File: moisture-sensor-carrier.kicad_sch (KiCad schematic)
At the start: 56 parts, among them J1 USB-C receptacle, J2 Battery - Adafruit 1578, J3 Solar panel, J4 SWD 10p 1.27mm, J5 Antenna feed, U1 nRF54L15-QFAA, U2 nPM1300-QEAA, U3 FDC1004, U4 SHT45-AD1F, X1 CM8V-T1A 32.768kHz CL=7pF 20p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, X2 FA-128 32MHz CL=8pF

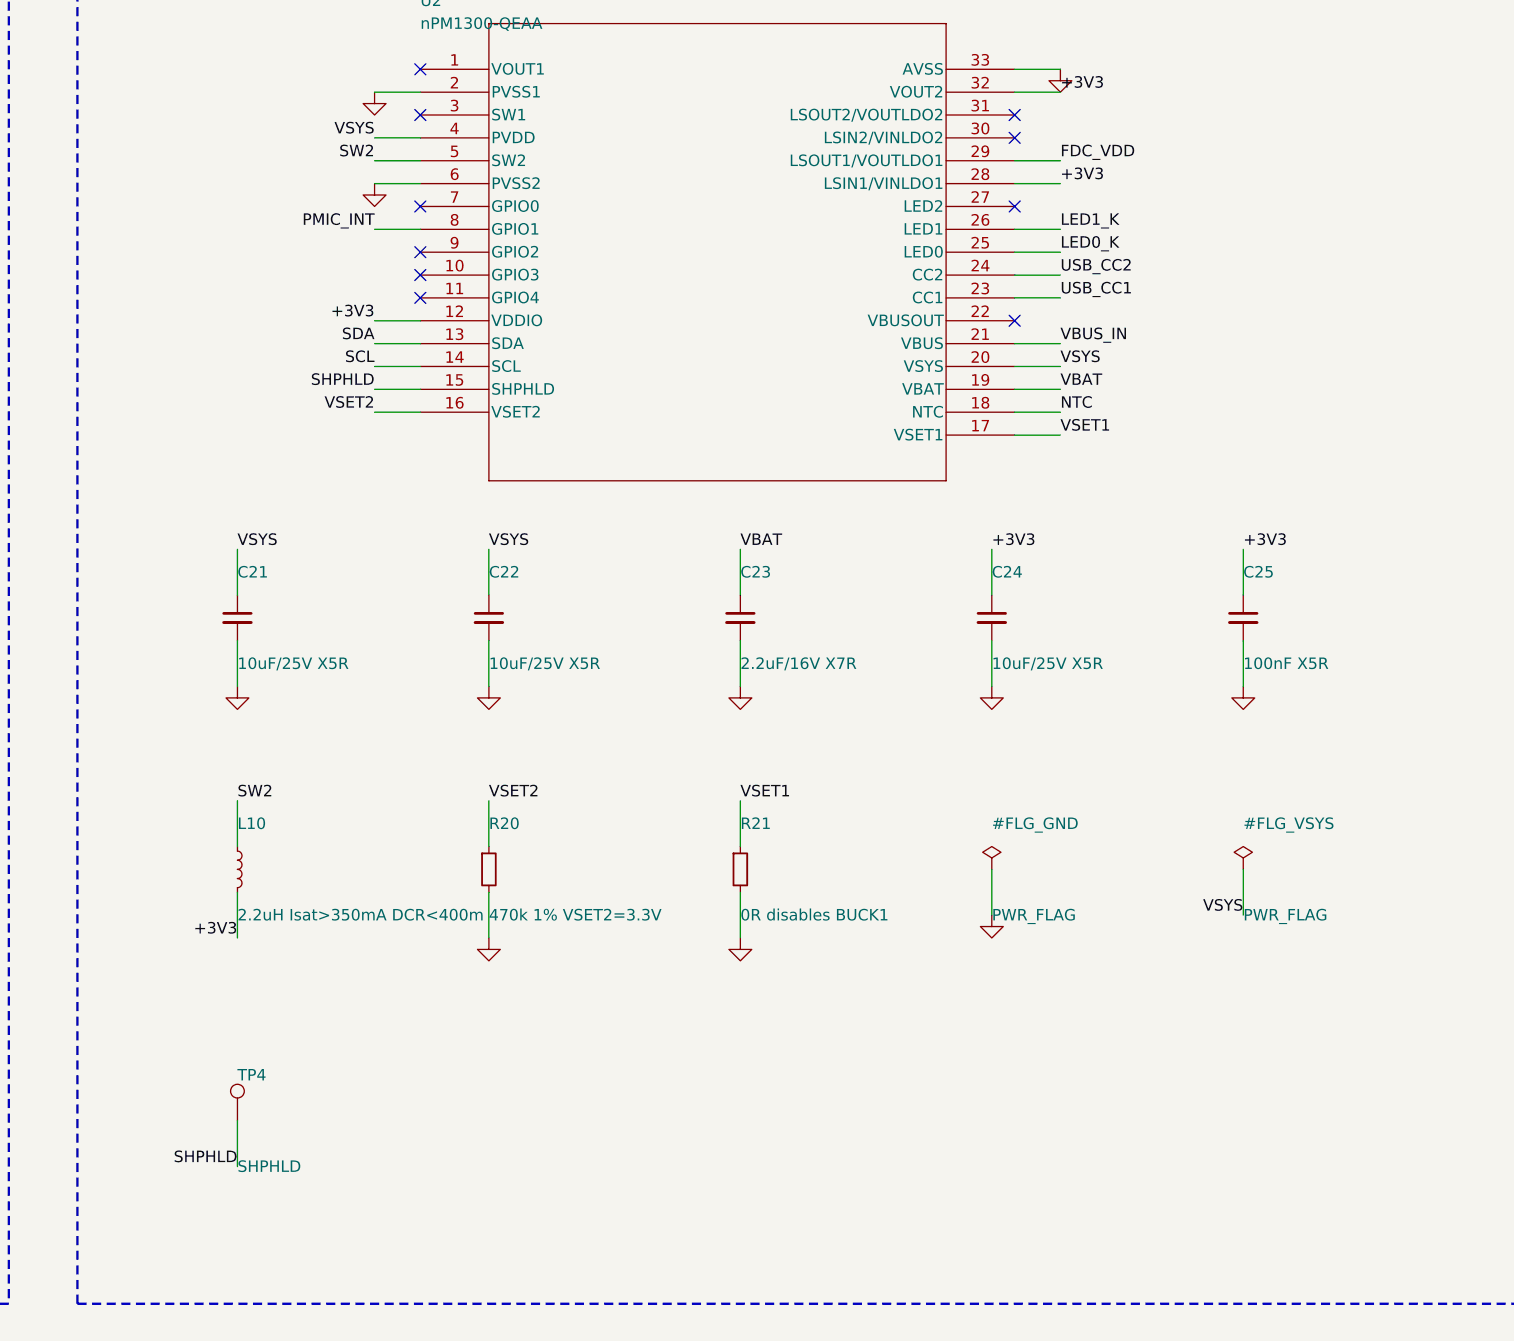
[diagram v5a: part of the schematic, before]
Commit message: PVSS2 net tie; fix DRU ordering that had disabled every width rule
Nordic's reference schematic (nPM1300 PS 9.3.2) annotates PVSS1 'Net tie'
and 'Via to GND-layer'. Pin 6 is BUCK2 power ground, not a general ground
pin. Split to /GND_PVSS2 carrying C24.2 and U2.6, rejoined by NT3 at the
via. C24 returns to it so the SW2 -> L10 -> C24 -> PVSS2 loop closes
locally rather than through the plane. PVSS1 stays on GND - BUCK1 is
disabled and carries nothing.

NT3 uses a new compact net tie: the stock 0.5 mm one does not fit the
0.69 mm gap between C24 and U2.

Separately, and more important: verifying the new width rule uncovered
that ORDERING had silently disabled every width rule in the file. 'Fab
minimum track' matches every track at 0.127 mm and sat at the bottom, so
under last-match-wins it was overriding 'Power track width', 'Charge path
width' and 'Switch node width'. A 0.3 mm track on a Power-class net
produced no violation at all. The fabrication floor now sits above the
specific rules and the PVSS2 rule below 'Power track width'. Re-verified
by injection: the correct rule now fires with the correct limit.

Co-Authored-By: Claude Opus 5 <noreply@anthropic.com>
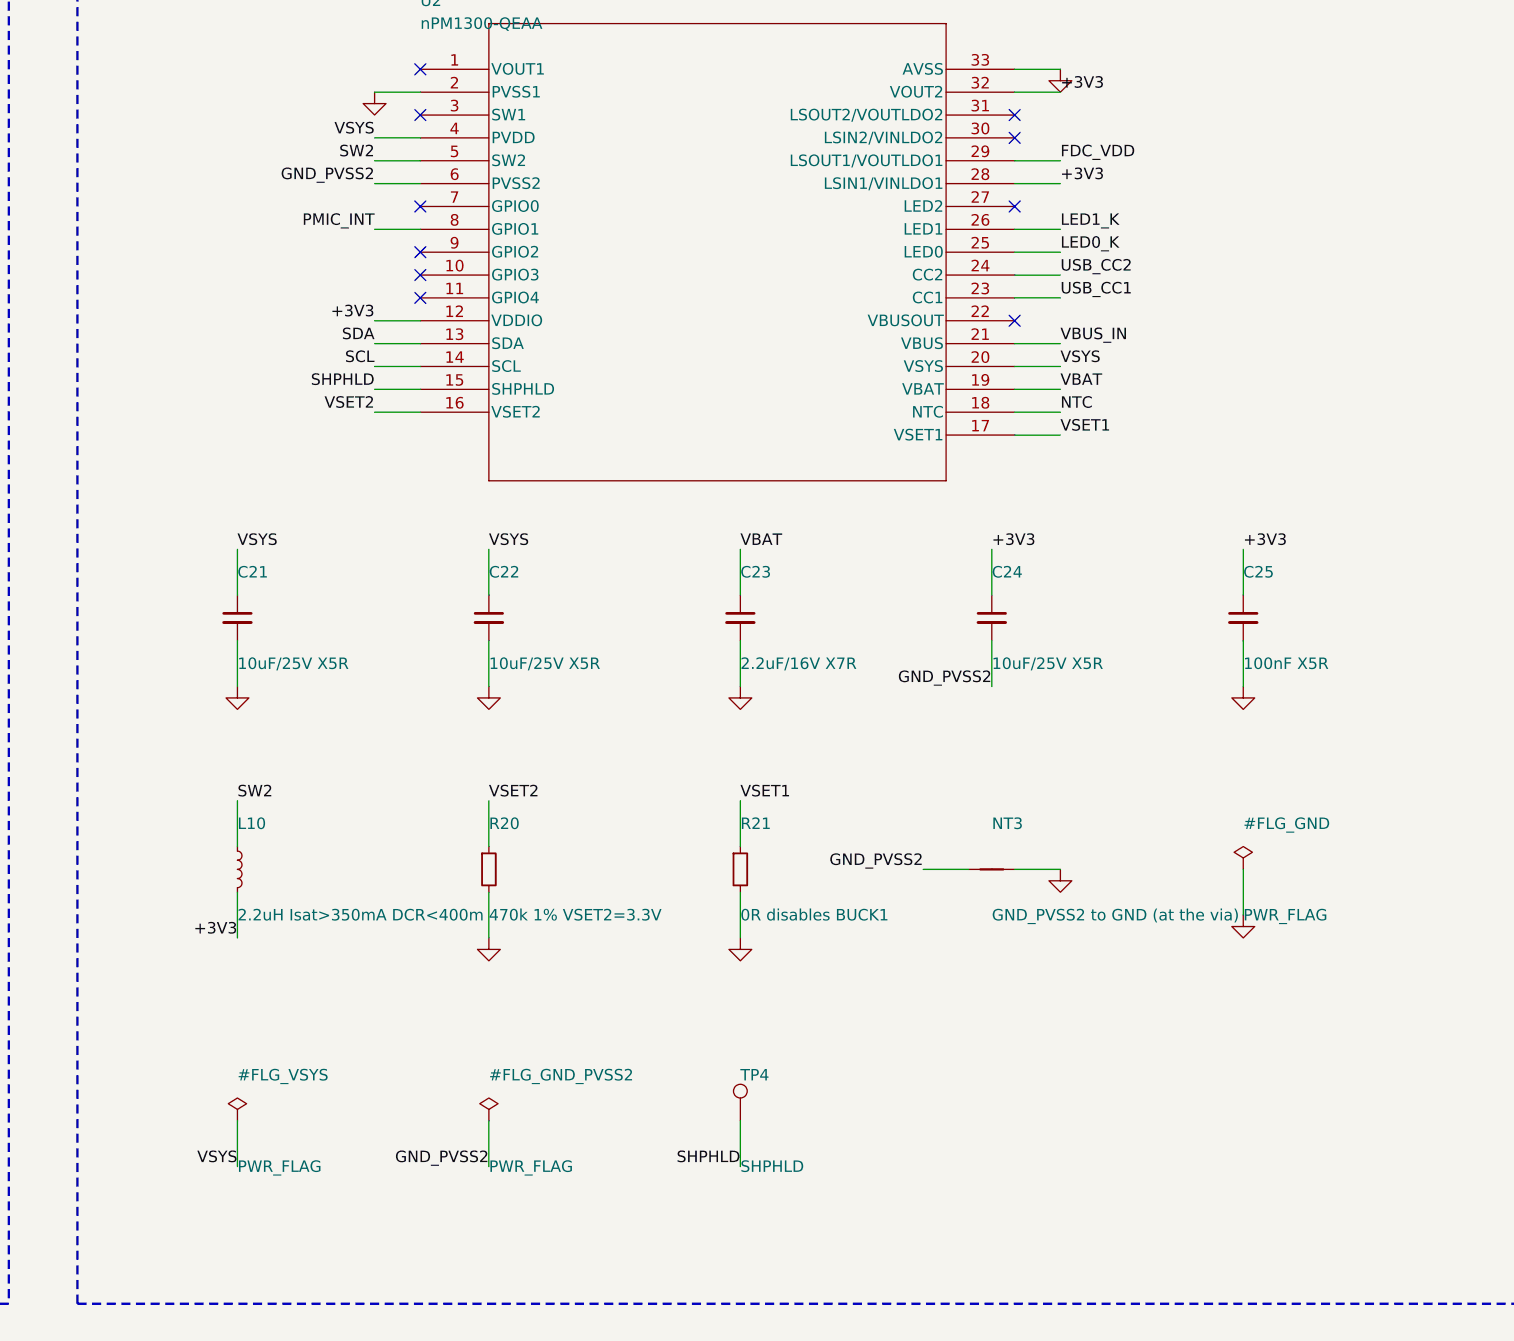
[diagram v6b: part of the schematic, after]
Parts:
- added NT3: GND_PVSS2 to GND (at the via), footprints:NetTie_Small, symbol Device:NetTie_2
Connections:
- net GND: now also NT3.2; no longer C24.2, U2.6 (PVSS2)
- new net GND_PVSS2: C24.2, NT3.1, U2.6 (PVSS2)
